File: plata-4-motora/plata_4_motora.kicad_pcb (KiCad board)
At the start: 2 copper layers, 120 x 84 mm, 27 parts, among them M0 мотор 0, M1 мотор 1, M2 мотор 2, M3 мотор 3, U0B S2209, U0T S2209, U1B S2209, U1T S2209, U2B S2209, U2T S2209, U3B S2209, U3T S2209

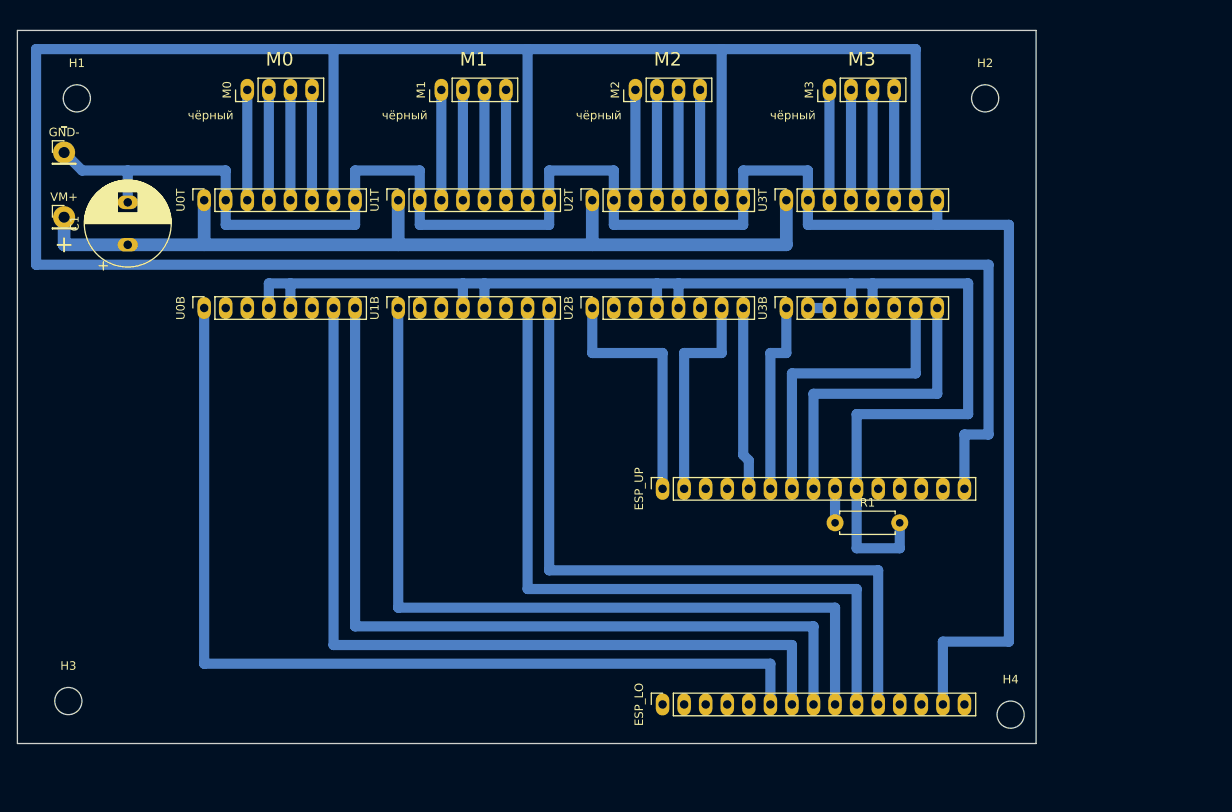
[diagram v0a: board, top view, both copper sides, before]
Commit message: Плата 4 моторов: PD-триггер модулем на гнёздах, GND к ESP по нижнему краю, 137x86; вики 9.3–9.6 с рендерами
Co-Authored-By: Claude Fable 5.1 <noreply@anthropic.com>
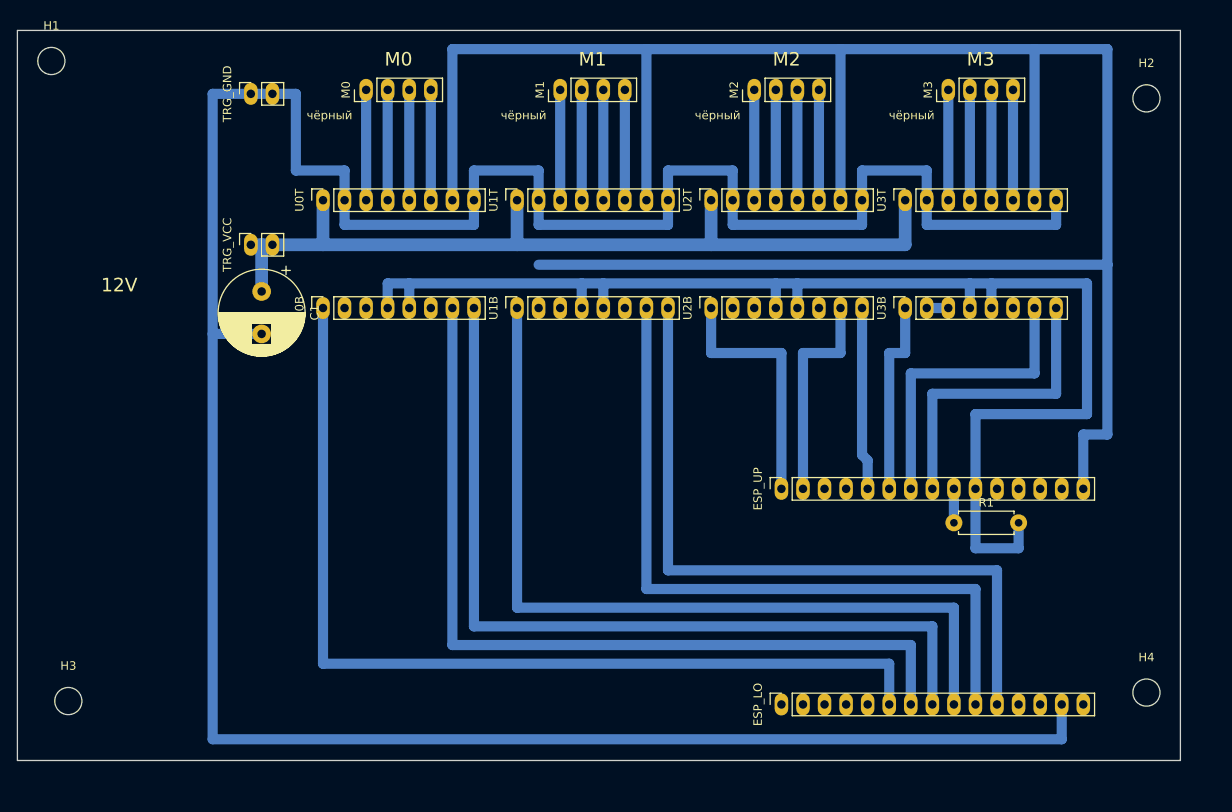
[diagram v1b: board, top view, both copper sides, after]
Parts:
- removed GND-: - от триггера, PinHeader_1x01_P2.54mm_Vertical
- removed VM+: + от триггера, PinHeader_1x01_P2.54mm_Vertical
- added TRG: , , F.Cu at (16.3, 16.4)
- added TRG_GND: триггер GND, PinSocket_1x02_P2.54mm_Vertical, F.Cu at (27.5, 7.47)
- added TRG_VCC: триггер VCC, PinSocket_1x02_P2.54mm_Vertical, F.Cu at (27.5, 25.2)
- moved H2 19.0 mm to (133.0, 8.00)
- moved C1 16.7 mm to (28.8, 30.8), turned to -90 degrees
- moved H4 16.2 mm to (133.0, 78.0)
- moved DRV0 14.0 mm to (44.9, 26.4)
- moved DRV1 14.0 mm to (67.8, 26.4)
- moved DRV2 14.0 mm to (90.6, 26.4)
- moved DRV3 14.0 mm to (113.5, 26.4)
- moved ESP 14.0 mm to (108.2, 66.7)
- moved ESP_LO 14.0 mm to (90.0, 79.4)
- moved ESP_UP 14.0 mm to (90.0, 54.0)
- moved M0 14.0 mm to (41.1, 7.00)
- moved M1 14.0 mm to (63.9, 7.00)
- moved M2 14.0 mm to (86.8, 7.00)
- moved M3 14.0 mm to (109.7, 7.00)
- moved R1 14.0 mm to (110.3, 58.0)
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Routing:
- net GND: track 227.9 -> 342.0 mm
- net VIO: track 344.2 -> 272.5 mm
- net VM: track 109.3 -> 103.6 mm
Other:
- board size 120 x 84 mm -> 137 x 86 mm
- board text added: "12V"
- board text removed: "+"
- board text removed: "-"

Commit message: Плата 4 моторов v3: оба разъёма на правом краю, триггер лежит на штырях насквозь; вики 9.3, 9.6
Co-Authored-By: Claude Fable 5.1 <noreply@anthropic.com>
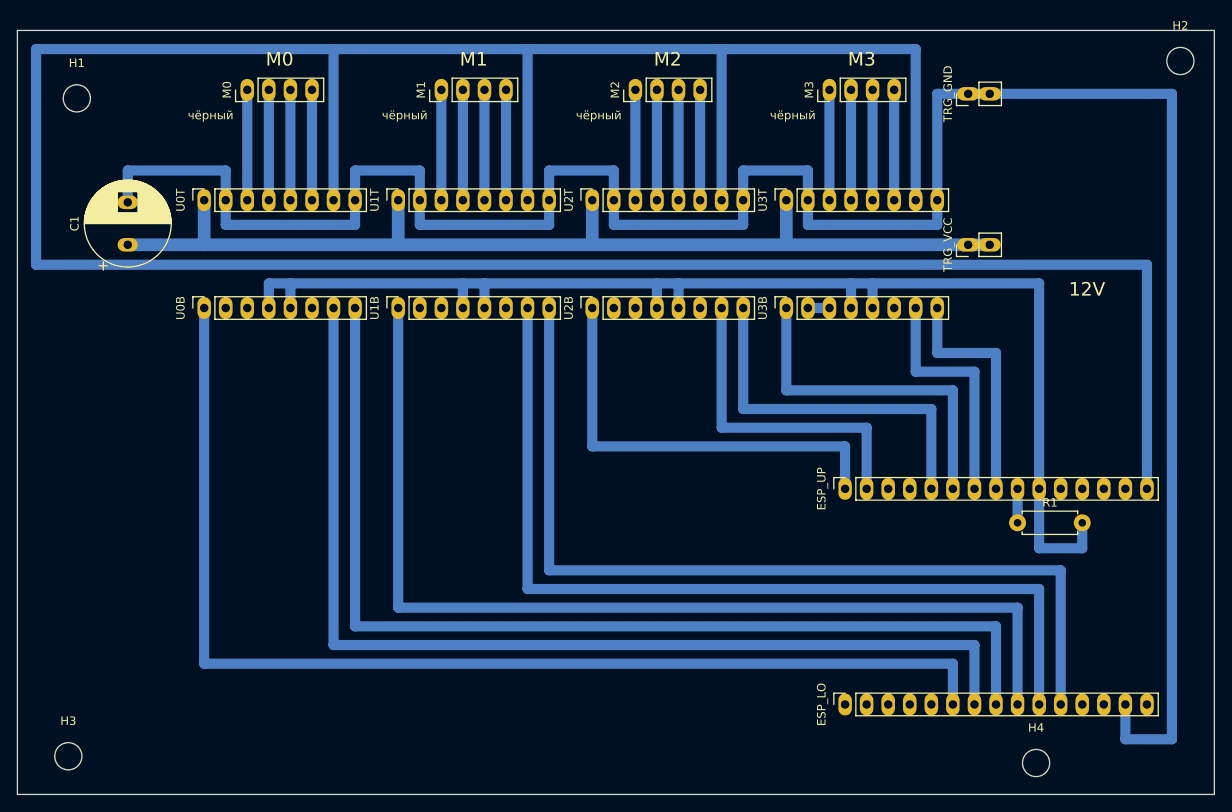
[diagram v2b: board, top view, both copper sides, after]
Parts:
- removed the TRG_GND at (27.5, 7.47)
- removed the TRG_VCC at (27.5, 25.2)
- added TRG_GND: триггер GND, PinHeader_1x02_P2.54mm_Vertical, F.Cu at (112.0, 7.47)
- added TRG_VCC: триггер VCC, PinHeader_1x02_P2.54mm_Vertical, F.Cu at (112.0, 25.2)
- moved TRG 109.4 mm to (125.7, 16.4)
- moved C1 16.7 mm to (13.0, 25.2), turned to 90 degrees
- moved H4 15.4 mm to (120.0, 86.3)
- moved DRV0 14.0 mm to (30.9, 26.4)
- moved DRV1 14.0 mm to (53.8, 26.4)
- moved DRV2 14.0 mm to (76.6, 26.4)
- moved DRV3 14.0 mm to (99.5, 26.4)
- moved M0 14.0 mm to (27.1, 7.00)
- moved M1 14.0 mm to (49.9, 7.00)
- moved M2 14.0 mm to (72.8, 7.00)
- moved M3 14.0 mm to (95.7, 7.00)
- moved U0B 14.0 mm to (22.0, 32.7)
- moved U0T 14.0 mm to (22.0, 20.0)
- moved U1B 14.0 mm to (44.9, 32.7)
- moved U1T 14.0 mm to (44.9, 20.0)
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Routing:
- net VIO: track 272.5 -> 360.0 mm
- net GND: track 342.0 -> 272.6 mm
- net DIR2: track 21.6 -> 43.5 mm
- net STEP0: track 100.7 -> 122.2 mm
- net STEP1: track 85.5 -> 107.0 mm
- net EN2: track 29.6 -> 51.1 mm
- net EN1: track 98.2 -> 119.7 mm
- net EN0: track 113.4 -> 134.9 mm
- net DIR1: track 85.5 -> 107.0 mm
- net DIR0: track 100.7 -> 122.2 mm
- net VM: track 103.6 -> 122.5 mm
- net EN3: track 23.2 -> 40.9 mm
- net STEP2: track 25.7 -> 38.4 mm
- net STEP3: track 35.9 -> 28.2 mm
- net DIR3: track 35.9 -> 28.2 mm
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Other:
- board size 137 x 86 mm -> 141 x 90 mm
